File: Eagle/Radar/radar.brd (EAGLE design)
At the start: 100 x 80 mm, 35 parts

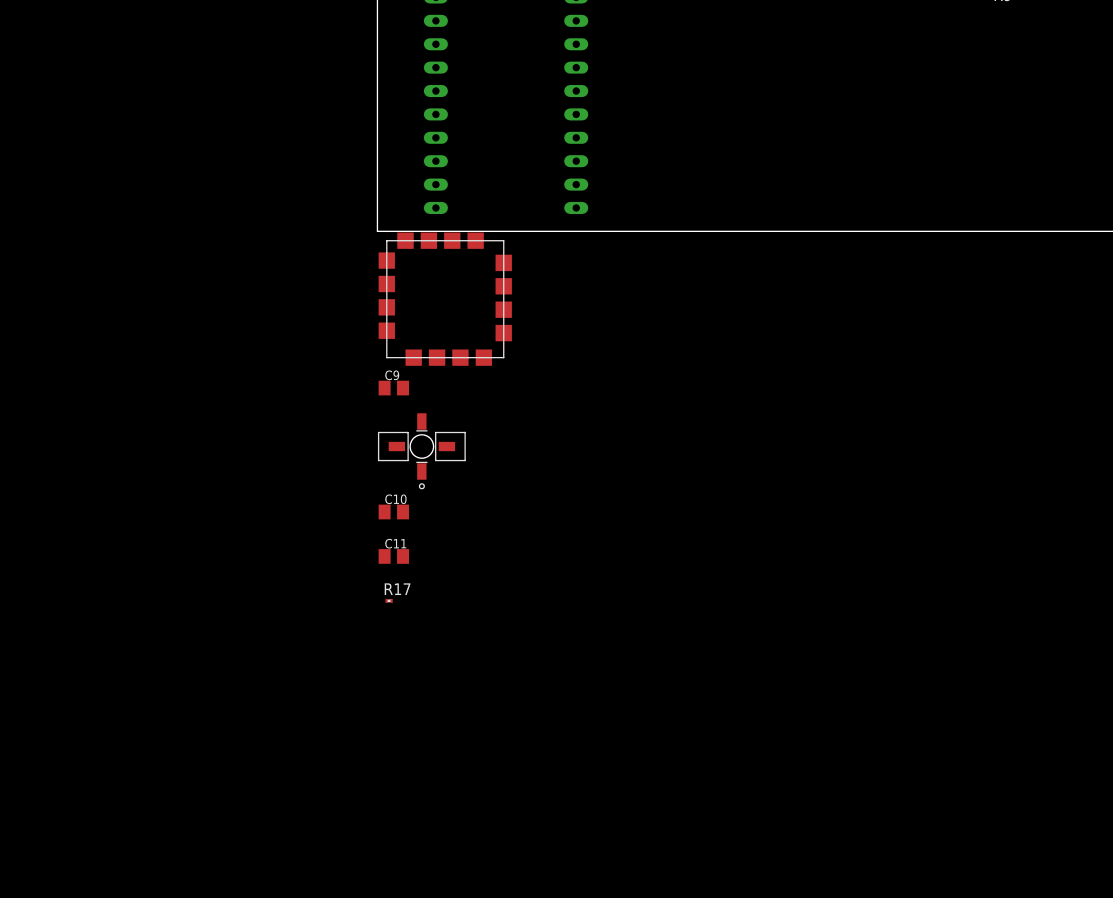
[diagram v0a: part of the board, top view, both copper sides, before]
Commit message: Added amplifier circuits, ground clips, 3.5mm
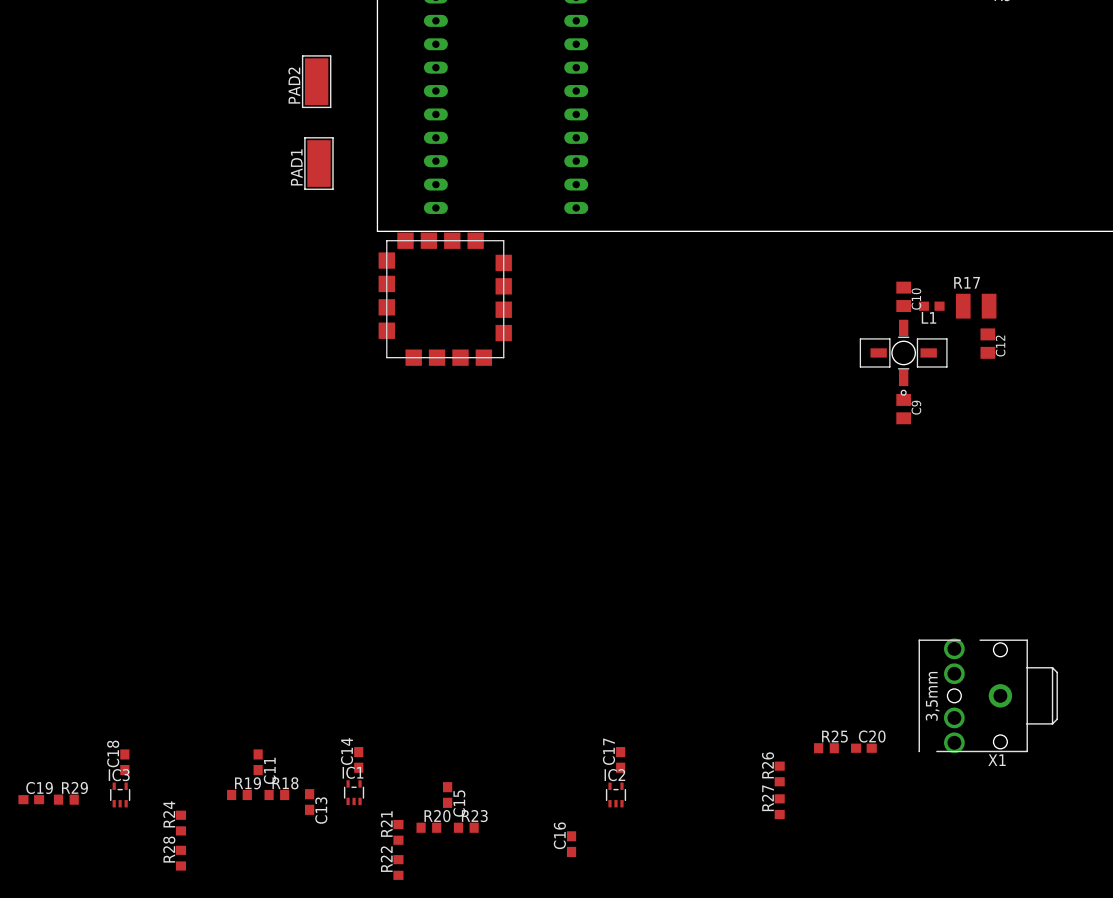
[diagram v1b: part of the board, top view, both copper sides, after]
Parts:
- added C12: 10uF, rcl:C0805K
- added C13, C14, C15, C16, C17, C18, C19, C20: (no value), rcl:C0603
- added IC1, IC2, IC3: AD8519KS, analog-devices:SC70-5
- added L1: 56 nH, radar:0603
- added PAD1, PAD2: WIREPADSMD5-2,5, wirepad:5-2,5
- added R18, R19, R20, R21, R22, R23, R24, R25, R26, R27, R28, R29: (no value), rcl:R0603
- added X1: STEREOJACK, adafruit:STX3100
- C11: value 10uF -> (none); device rcl:C0805K -> rcl:C0603
- R17: value 0 -> 191, 1/2W; device rcl:R0201 -> rcl:R1210
- moved R17 71.3 mm to (65.0, -8.13)
- moved C10 60.1 mm to (57.1, -7.11), turned to 270 degrees
- moved C9 55.4 mm to (57.1, -19.3), turned to 270 degrees
- moved U$8 53.3 mm to (57.1, -13.2)
- moved C11 26.8 mm to (-13.0, -57.7), turned to 270 degrees
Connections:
- new net N$1: C20.1, R25.2
- new net N$10: IC3.1, R19.1, R24.2
- new net N$11: IC3.4, R24.1, R28.2
- new net N$12: C19.2, IC3.3, R29.2
- new net N$13: C19.1
- new net N$14: C20.2, X1.2
- new net N$2: C11.2, R18.1, R19.2
- new net N$3: C11.1, C15.1, IC1.1, IC2.1, R20.1, R21.2, R25.1, R26.2
- new net N$6: C13.1, C16.1, IC1.3, IC2.3, R18.2, R23.2
- new net N$7: C14.1, C17.1, C18.1, IC1.5, IC2.5
- new net N$8: IC1.4, IC2.4, R21.1, R22.2, R26.1, R27.2
- new net N$9: C15.2, R20.2, R23.1
- net AMP_OUT: now also L1.2
- net AMP_VCC: now also L1.1; no longer C11.1
- net GND: now also C12.2, C13.2, C14.2, C16.2, C17.2, C18.2, IC1.2, IC2.2, IC3.2, PAD1.1, PAD2.1, R22.1, R27.1, R28.1, R29.1, X1.1; no longer C11.2
- net PP10V: now also C12.1

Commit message: Updated schematic
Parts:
- removed IC1, IC2, IC3: AD8519KS, analog-devices:SC70-5
- added C21, C22: 10uF, rcl:C0805K
- added C23: 0.1u, rcl:C0603
- added IC4: MAX414ESD, radar:SO14
- added JP1: (no value), pinhead:1X02
- added R30: 0, rcl:R0402
- added R31: 50, rcl:R0603
- added U$10: DMN3067LW-7, radar:SOT323
- added U$9: COUPLER, radar:COUPLER
- added X2, X3, X4: BU-SMA-G, radar:BU-SMA-G
- C14, C19: value (none) -> 10uF; device rcl:C0603 -> rcl:C0805K
- C17: value (none) -> 270p; device rcl:C0603 -> rcl:C0603K
- C18: value (none) -> 0.1u
- R2, R5, R8: device rcl:R0201 -> rcl:R0402
- U$7: value CVCO55CC-2380-2580 -> MAX268X; device radar:CVCO55CC-2380-2580 -> radar:SOT23-6
- moved C17 91.4 mm to (-37.3, -122.9), turned to 0 degrees
- moved C19 78.5 mm to (-37.3, -140.2)
- moved U$7 71.0 mm to (-37.1, -73.7)
- moved C14 70.2 mm to (-37.3, -118.1), turned to 0 degrees
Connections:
- net N$1 renamed AUD1_AC
- net N$14 renamed AUD1_OUT
- net N$2 renamed LFA2_IN
- net N$9 renamed LFA3_IN
- removed net N$10: IC3.1, R19.1, R24.2
- removed net N$11: IC3.4, R24.1, R28.2
- removed net N$12: C19.2, IC3.3, R29.2
- removed net N$13: C19.1
- removed net N$3: C11.1, C15.1, IC1.1, IC2.1, R20.1, R21.2, R25.1, R26.2
- removed net N$4: C9.2
- removed net N$5: C10.1
- removed net N$6: C13.1, C16.1, IC1.3, IC2.3, R18.2, R23.2
- removed net N$7: C14.1, C17.1, C18.1, IC1.5, IC2.5
- removed net N$8: IC1.4, IC2.4, R21.1, R22.2, R26.1, R27.2
- removed net VCO_RF: U$7.10
- removed net VCO_VT: U$7.2
- new net COUPLER_COUPLED: C14.2, U$9.1
- new net COUPLER_IN: C10.1, U$9.4
- new net COUPLER_ISO: R31.2, U$9.2
- new net COUPLER_OUT: U$9.3, X4.1
- new net LFA1_+: C19.1, IC4.3, R29.2
- new net LFA1_-: IC4.2, R24.1, R28.2
- new net LFA1_OUT: IC4.1, R19.1, R24.2
- new net LFA2_+: C13.1, IC4.5, R18.2
- new net LFA2_-: IC4.6, R21.1, R22.2
- new net LFA2_OUT: C11.1, IC4.7, R20.1, R21.2
- new net LFA3_+: C16.1, IC4.10, R23.2
- new net LFA3_-: IC4.9, R26.1, R27.2
- new net LFA3_OUT: C15.1, IC4.8, R25.1, R26.2
- new net MAX268X_SHDN: R30.1, U$7.6
- new net MIXER_IF: C19.2, U$7.4
- new net MIXER_LO: C14.1, U$7.1
- new net MIXER_RF: C17.1, U$7.3
- new net MOTOR_CTRL: U$10.1, U$3.D6
- new net N$1: JP1.2, U$10.3
- new net PLL_OUT: C9.2, X2.1
- new net RF_RX: C17.2, X3.1
- net GND: now also C21.2, C22.2, C23.2, IC4.11, R31.1, U$10.2, U$7.2, X2.2, X2.3, X2.4, X2.5, X3.2, X3.3, X3.4, X3.5, X4.2, X4.3, X4.4, X4.5; no longer C14.2, C17.2, IC1.2, IC2.2, IC3.2, U$7.1, U$7.11, U$7.12, U$7.13, U$7.15, U$7.16, U$7.3, U$7.4, U$7.5, U$7.6, U$7.7, U$7.8, U$7.9
- net PP10V: now also C18.1, C22.1, IC4.4
- net PP5V: now also C21.1, C23.1, R30.2, U$7.5; no longer U$7.14
- net PPUSB: now also JP1.1

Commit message: Updated digi values
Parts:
- removed C7, C8: 10uF, rcl:C0805K
- removed R10: 4.48k, rcl:R0603
- removed R15, R16: 0, rcl:R0603
- removed R9: 2.61k, rcl:R0603
- removed U$6: TPS73801, radar:SOT223-6
- added L2: 1.2nH, radar:0603
- added R32: 28k, rcl:R0603
- C11, C13, C15, C16: value (none) -> 1n
- C20: value (none) -> 10uF; device rcl:C0603 -> rcl:C0805K
- R18: value (none) -> 7.15k
- R19: value (none) -> 8.25k
- R20: value (none) -> 17.4k
- R21, R26: value (none) -> 1k
- R22: value (none) -> 12.1k
- R23: value (none) -> 4.12k
- R24: value (none) -> 100k
- R25: value (none) -> 0
- R27: value (none) -> 1.2k
- R28: value (none) -> 200
- R29: value (none) -> 10k
- R8: value 0 -> 20k; device rcl:R0402 -> pot:B25P
- moved R8 269.5 mm to (-43.4, -212.1)
- moved C20 183.0 mm to (-37.3, -215.4)
- moved R24 142.4 mm to (-37.6, -205.7), turned to 0 degrees
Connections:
- removed net LDO3_EN: R8.2, U$6.5
- removed net LDO3_FB: R10.1, R9.2, U$6.4
- removed net LDO3_IN: C7.1, R15.2, R8.1, U$6.1
- removed net LDO3_OUT: C8.1, R10.2, R16.1, U$6.2
- removed net PP3V3: R16.2
- net GND: now also L2.2; no longer C13.2, C16.2, C7.2, C8.2, R22.1, R27.1, R28.1, R29.1, R9.1, U$6.3, U$6.6
- net LFA1_-: now also R8.A, R8.S; no longer R24.1
- net LFA1_OUT: now also R8.E; no longer R24.2
- net LFA2_IN: now also R24.2
- net LFA3_IN: now also R32.2
- net PP5V: now also C13.2, C16.2, R22.1, R24.1, R27.1, R28.1, R29.1, R32.1; no longer R15.1
- net RF_RX: now also L2.1

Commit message: Finalized sch
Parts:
- added C7: 10uF, rcl:C0805K
- added JP2: (no value), pinhead:1X04
- added JP3: (no value), pinhead:1X02
- added L3: 56 nH, radar:0603
- added U$6: COUPLER, radar:COUPLER
- U$9: value COUPLER -> PAT1220; device radar:COUPLER -> radar:PAT1220
- moved U$9 124.2 mm to (-44.5, -233.7)
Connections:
- new net AUD2_OUT: C7.2, X1.5
- new net AUD2_PLACEHOLDER: C7.1
- new net ENCODER_A: JP2.2
- new net ENCODER_B: JP2.3, U$3.D2
- new net N$2: C9.2, U$9.2
- net COUPLER_COUPLED: now also U$6.1; no longer U$9.1
- net COUPLER_IN: now also U$6.4; no longer U$9.4
- net COUPLER_ISO: now also U$6.2; no longer U$9.2
- net COUPLER_OUT: now also U$6.3; no longer U$9.3
- net GND: now also JP2.4, JP3.2, U$9.3
- net MIXER_IF: now also L3.2
- net PLL_OUT: now also U$9.1; no longer C9.2
- net PP5V: now also JP2.1, L3.1
- net PPUSB: now also JP3.1
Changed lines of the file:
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@@
 <attribute name="DIGI" value="MAX414ESD+-ND" x="-32.512" y="-90.932" size="1.778" layer="27" display="off"/>
-</element>
-<element name="U$9" library="radar" package="COUPLER" value="COUPLER" x="-36.322" y="-109.728">
-<attribute name="DIGI" value="HHM2917B1" x="-36.322" y="-109.728" size="1.778" layer="27" display="off"/>
 </element>
 <element name="R31" library="rcl" package="R0603" value="50" x="-37.592" y="-113.284">
@@
 <element name="JP1" library="pinhead" package="1X02" value="" x="-35.814" y="-196.342"/>
 <element name="L2" library="radar" package="0603" value="1.2nH" x="-37.338" y="-200.914">
-<attribute name="DIGI" value="712-1443-1-ND" x="-37.338" y="-200.914" size="1.778" layer="27" display="off"/>
+<attribute name="DIGI" value="535-11530-1-ND" x="-37.338" y="-200.914" size="1.778" layer="27" display="off"/>
 </element>
 <element name="R24" library="rcl" package="R0603" value="100k" x="-37.592" y="-205.74">
@@
 <attribute name="DIGI" value="3362P-203LF-ND" x="-43.434" y="-212.09" size="1.778" layer="27" display="off"/>
 </element>
+<element name="U$6" library="radar" package="COUPLER" value="COUPLER" x="-44.45" y="-219.964">
+<attribute name="DIGI" value="445-172645-1-ND" x="-44.45" y="-219.964" size="1.778" layer="27" display="off"/>
+</element>
+<element name="L3" library="radar" package="0603" value="56 nH" x="-45.466" y="-223.52">
+<attribute name="DIGI" value="712-1443-1-ND" x="-45.466" y="-223.52" size="1.778" layer="27" display="off"/>
+</element>
+<element name="C7" library="rcl" package="C0805K" value="10uF" x="-45.212" y="-228.346">
+<attribute name="DIGI" value="587-2985-1-ND" x="-45.212" y="-228.346" size="1.778" layer="27" display="off"/>
+</element>
+<element name="U$9" library="radar" package="PAT1220" value="PAT1220" x="-44.45" y="-233.68">
+<attribute name="DIGI" value="PAT123CT-ND" x="-44.45" y="-233.68" size="1.778" layer="27" display="off"/>
+</element>
+<element name="JP2" library="pinhead" package="1X04" value="" x="-41.402" y="-238.252"/>
+<element name="JP3" library="pinhead" package="1X02" value="" x="-43.942" y="-243.84"/>
 </elements>
 <signals>
@@
 <contactref element="U$10" pad="2"/>
 <contactref element="L2" pad="2"/>
+<contactref element="U$9" pad="3"/>
+<contactref element="JP2" pad="4"/>
+<contactref element="JP3" pad="2"/>
 <wire x1="-37.196" y1="-192.162" x2="-36.488" y2="-200.914" width="0" layer="19" extent="1-1"/>
 <wire x1="-36.488" y1="-187.198" x2="-37.196" y2="-192.162" width="0" layer="19" extent="1-1"/>
@@
 <wire x1="-37.084" y1="-74.81" x2="-36.338" y2="-79.248" width="0" layer="19" extent="1-1"/>
 <wire x1="-27.432" y1="-56.808" x2="-37.084" y2="-74.81" width="0" layer="19" extent="1-1"/>
+<wire x1="-44.45" y1="-234.03" x2="-36.488" y2="-200.914" width="0" layer="19" extent="1-1"/>
+<wire x1="-37.592" y1="-238.252" x2="-44.45" y2="-234.03" width="0" layer="19" extent="1-1"/>
+<wire x1="-42.672" y1="-243.84" x2="-37.592" y2="-238.252" width="0" layer="19" extent="1-1"/>
 <wire x1="-6.35" y1="7.366" x2="-27.432" y2="-56.808" width="0" layer="19" extent="1-1"/>
 <wire x1="-6.604" y1="16.256" x2="-6.35" y2="7.366" width="0" layer="19" extent="1-1"/>
@@
 <contactref element="C1" pad="+"/>
 <contactref element="JP1" pad="1"/>
+<contactref element="JP3" pad="1"/>
+<wire x1="-45.212" y1="-243.84" x2="-37.084" y2="-196.342" width="0" layer="19" extent="1-1"/>
 <wire x1="21.59" y1="30.48" x2="-37.084" y2="-196.342" width="0" layer="19" extent="1-1"/>
 <wire x1="20.922" y1="49.53" x2="21.59" y2="30.48" width="0" layer="19" extent="1-1"/>
@@
 <contactref element="R32" pad="1"/>
 <contactref element="R27" pad="1"/>
+<contactref element="L3" pad="1"/>
+<contactref element="JP2" pad="1"/>
 <wire x1="-38.442" y1="-205.74" x2="-38.442" y2="-210.566" width="0" layer="19" extent="1-1"/>
+<wire x1="-46.316" y1="-223.52" x2="-38.442" y2="-210.566" width="0" layer="19" extent="1-1"/>
+<wire x1="-45.212" y1="-238.252" x2="-46.316" y2="-223.52" width="0" layer="19" extent="1-1"/>
 <wire x1="-38.188" y1="-187.198" x2="-38.442" y2="-205.74" width="0" layer="19" extent="1-1"/>
 <wire x1="-36.942" y1="-84.074" x2="-38.188" y2="-187.198" width="0" layer="19" extent="1-1"/>
@@
 </signal>
 <signal name="PLL_OUT">
-<contactref element="C9" pad="2"/>
 <contactref element="X2" pad="1"/>
-<wire x1="57.15" y1="-20.304" x2="-35.052" y2="-148.844" width="0" layer="19" extent="1-1"/>
+<contactref element="U$9" pad="1"/>
+<wire x1="-45.2" y1="-232.83" x2="-35.052" y2="-148.844" width="0" layer="19" extent="1-1"/>
 </signal>
 <signal name="COUPLER_IN">
 <contactref element="C10" pad="1"/>
-<contactref element="U$9" pad="4"/>
-<wire x1="57.15" y1="-6.112" x2="-36.672" y2="-109.453" width="0" layer="19" extent="1-1"/>
+<contactref element="U$6" pad="4"/>
+<wire x1="-44.8" y1="-219.689" x2="57.15" y2="-6.112" width="0" layer="19" extent="1-1"/>
 </signal>
 <signal name="AMP_VCC">
@@
 <contactref element="U$7" pad="4"/>
 <contactref element="C19" pad="2"/>
+<contactref element="L3" pad="2"/>
 <wire x1="-36.134" y1="-72.51" x2="-36.338" y2="-140.208" width="0" layer="19" extent="1-1"/>
+<wire x1="-44.616" y1="-223.52" x2="-36.338" y2="-140.208" width="0" layer="19" extent="1-1"/>
 </signal>
 <signal name="MIXER_RF">
@@
 </signal>
 <signal name="COUPLER_OUT">
-<contactref element="U$9" pad="3"/>
 <contactref element="X4" pad="1"/>
-<wire x1="-35.972" y1="-109.453" x2="-35.052" y2="-173.736" width="0" layer="19" extent="1-1"/>
+<contactref element="U$6" pad="3"/>
+<wire x1="-44.1" y1="-219.689" x2="-35.052" y2="-173.736" width="0" layer="19" extent="1-1"/>
 </signal>
 <signal name="COUPLER_ISO">
-<contactref element="U$9" pad="2"/>
 <contactref element="R31" pad="2"/>
-<wire x1="-35.972" y1="-110.003" x2="-36.742" y2="-113.284" width="0" layer="19" extent="1-1"/>
+<contactref element="U$6" pad="2"/>
+<wire x1="-44.1" y1="-220.239" x2="-36.742" y2="-113.284" width="0" layer="19" extent="1-1"/>
 </signal>
 <signal name="COUPLER_COUPLED">
-<contactref element="U$9" pad="1"/>
 <contactref element="C14" pad="2"/>
-<wire x1="-36.672" y1="-110.003" x2="-36.338" y2="-118.11" width="0" layer="19" extent="1-1"/>
+<contactref element="U$6" pad="1"/>
+<wire x1="-44.8" y1="-220.239" x2="-36.338" y2="-118.11" width="0" layer="19" extent="1-1"/>
 </signal>
 <signal name="RF_RX">
@@
 <wire x1="6.35" y1="17.78" x2="-38.496" y2="-192.162" width="0" layer="19" extent="1-1"/>
 </signal>
+<signal name="AUD2_OUT">
+<contactref element="C7" pad="2"/>
+<contactref element="X1" pad="5"/>
+<wire x1="-44.212" y1="-228.346" x2="62.658" y2="-45.346" width="0" layer="19" extent="1-1"/>
+</signal>
+<signal name="AUD2_PLACEHOLDER">
+<contactref element="C7" pad="1"/>
+</signal>
+<signal name="N$2">
+<contactref element="U$9" pad="2"/>
+<contactref element="C9" pad="2"/>
+<wire x1="-43.7" y1="-232.83" x2="57.15" y2="-20.304" width="0" layer="19" extent="1-1"/>
+</signal>
+<signal name="ENCODER_B">
+<contactref element="JP2" pad="3"/>
+<contactref element="U$3" pad="D2"/>
+<wire x1="-40.132" y1="-238.252" x2="6.35" y2="27.94" width="0" layer="19" extent="1-1"/>
+</signal>
+<signal name="ENCODER_A">
+<contactref element="JP2" pad="2"/>
+</signal>
 </signals>
